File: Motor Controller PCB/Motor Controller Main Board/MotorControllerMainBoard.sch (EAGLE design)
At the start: 79 parts, among them T1 TEENSY_3.1_ALL_PINS

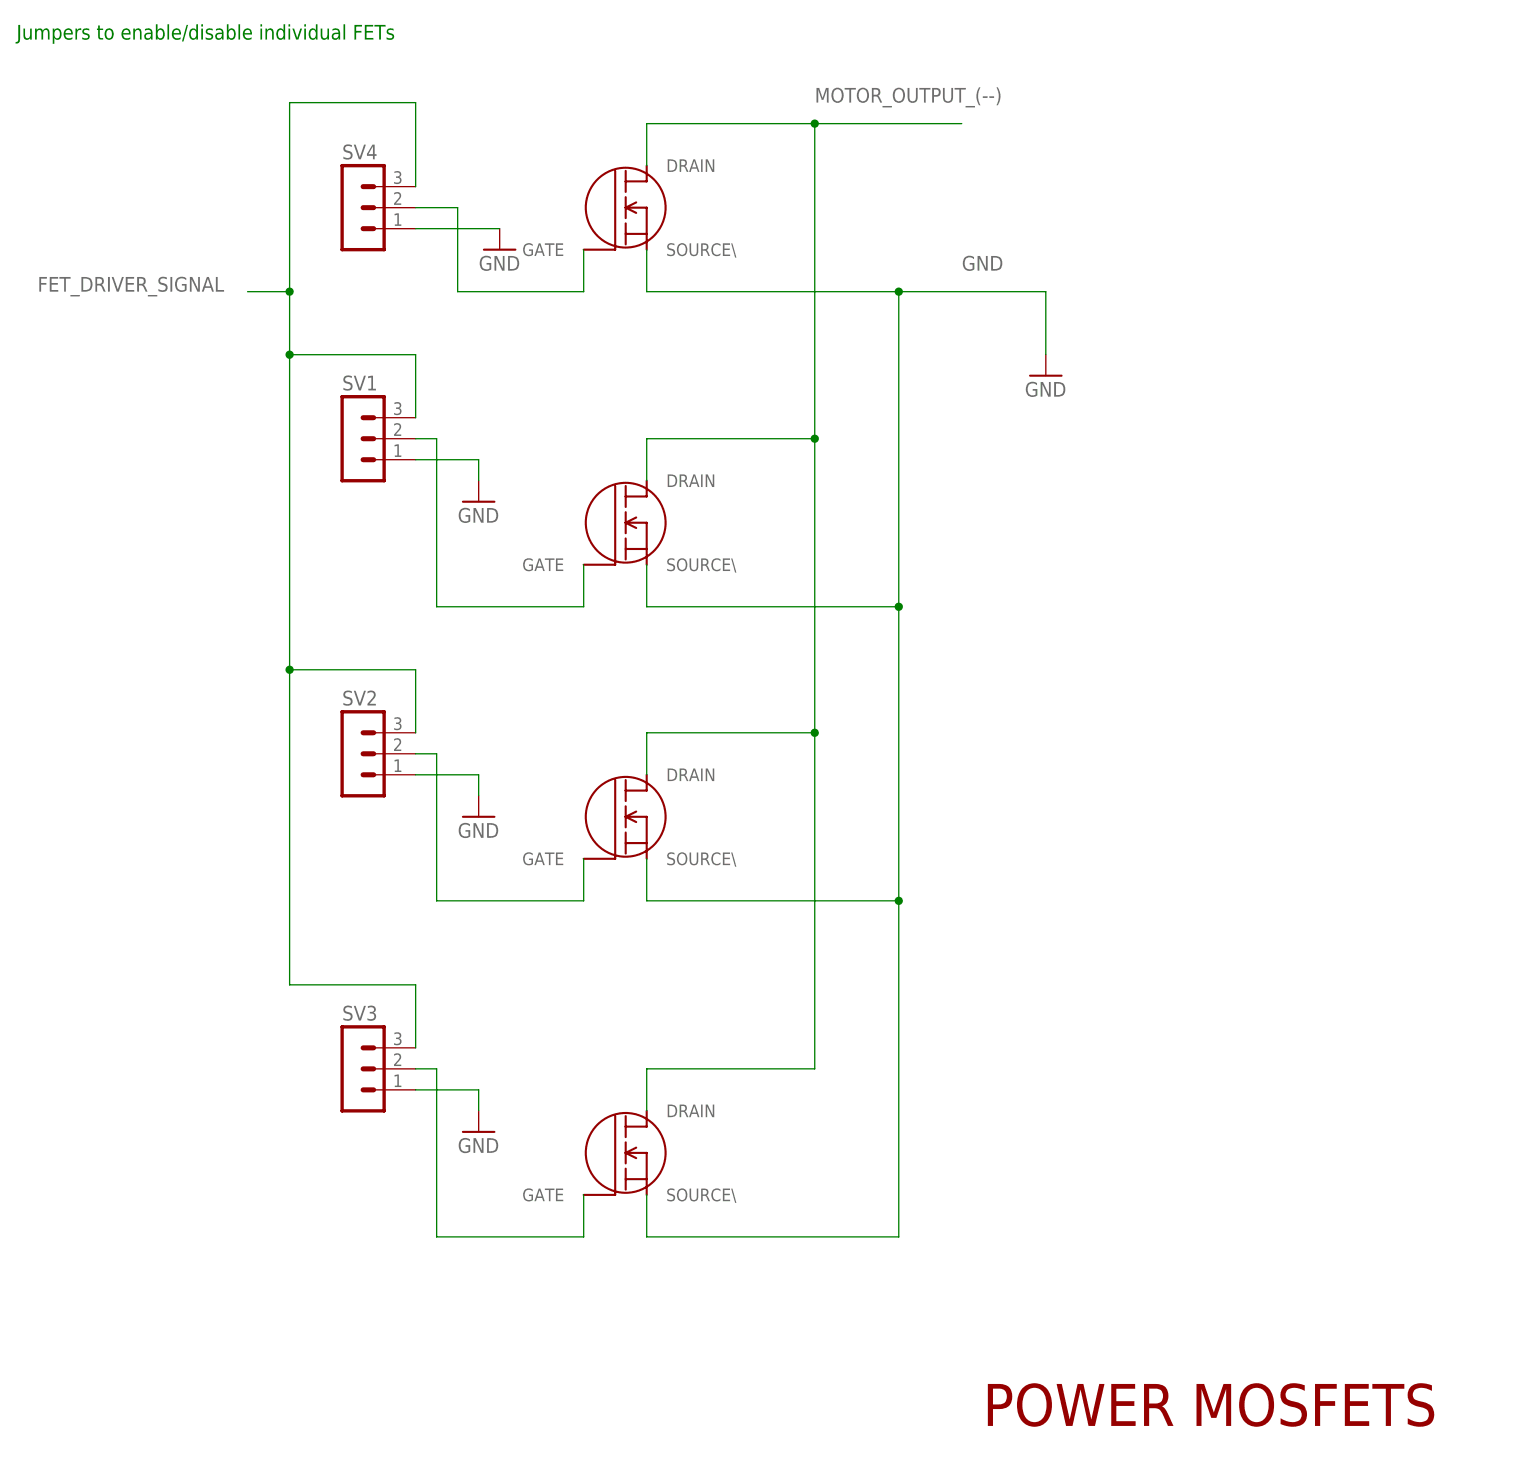
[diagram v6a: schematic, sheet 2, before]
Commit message: Added gate resistors
-4.7ohm on each FET
-Helps reduce ringing
-Helps deal with slight difference in capacitance so that they turn on
closer to at the same time.
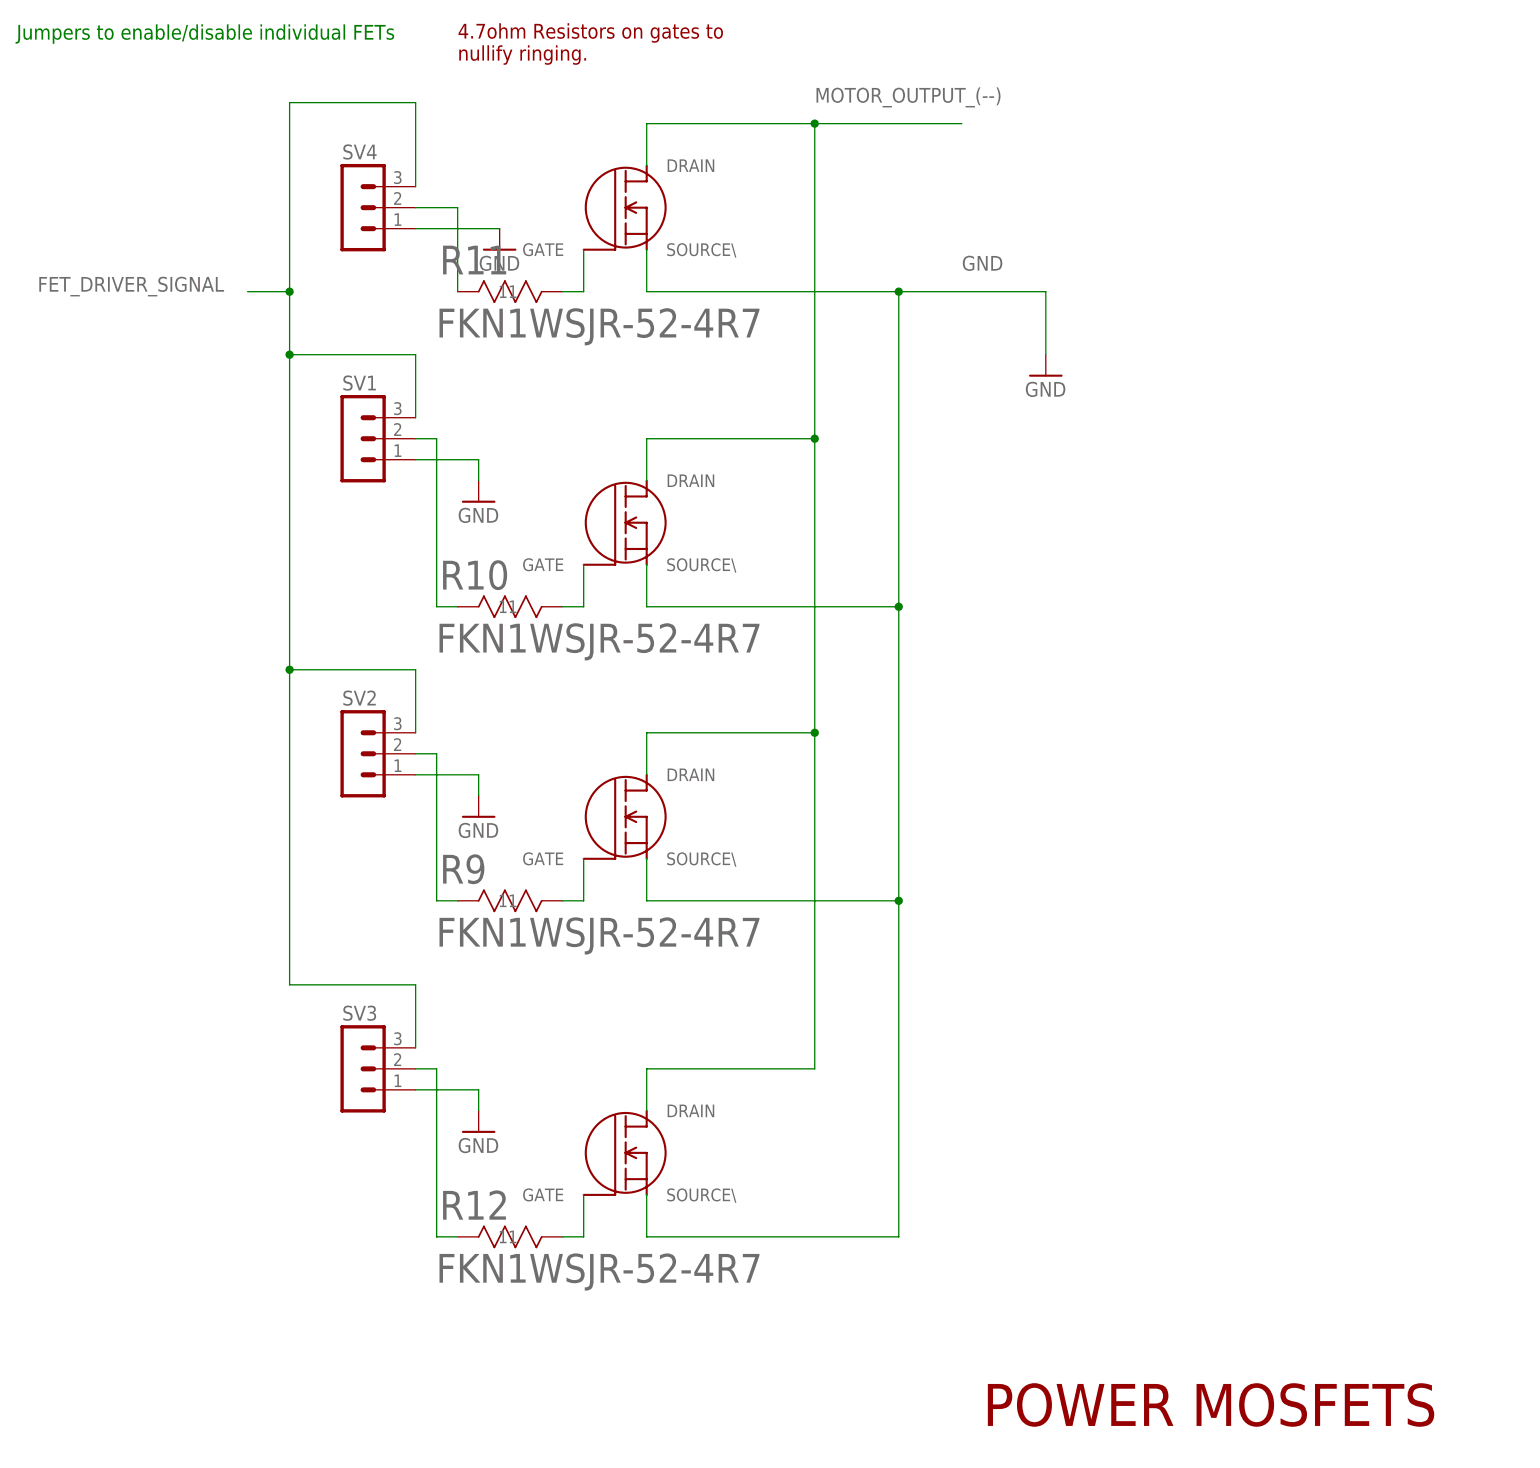
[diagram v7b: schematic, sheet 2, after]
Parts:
- added R10, R11, R12, R9: FKN1WSJR-52-4R7, MotorControllerEagleLibrary:FKN1WSJR-52-4R7
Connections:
- new net N$10: R11.22, U$1.GATE
- new net N$11: R9.22, U$3.GATE
- new net N$12: R12.22, U$4.GATE
- new net N$2: R10.22, U$2.GATE
- net FET_DRIVER_SIGNAL: now also R9.11; no longer U$3.GATE
- net N$3: now also R10.11; no longer U$2.GATE
- net N$5: now also R12.11; no longer U$4.GATE
- net N$8: now also R11.11; no longer U$1.GATE
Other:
- note added: "4.7ohm Resistors on gates to nullify ringing."
- note added: "Future Revision will have circuit protection in this block"
